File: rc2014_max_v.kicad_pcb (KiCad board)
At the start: 4 copper layers, 101.6 x 50.8 mm, 128 parts, among them J1 M3 Mounting Hole, J2 Conn_01x40, J3 Conn_01x24, J4 USB_B_Micro, J5 AVR-JTAG-10, J6 Pro Bus, J7 PMOD1, J8 PMOD2, J9 UPDI TTL, SW1 SW_Push, SW2 SW_Push, U1 TXB0108PWR, U10 ATtiny1614-SS, U11 5M1270ZT144C5N, U12 93LC46BT-I/OT, U13 IS61LV5128AL-10TLI, U14 Si5351A-B-GT, U15 TXB0108PWR, U16 TXB0108PWR, U17 MIC5356-SGYMME, U2 TXB0108PWR, U3 TXB0108PWR, U4 TXB0108PWR, U5 TXB0108PWR, U6 TXB0108PWR, U7 TXB0108PWR, U8 TPD2EUSB30, U9 FT2232H, X1 KC5032K12.0000C10E00, Y1 25MHZ 8PF

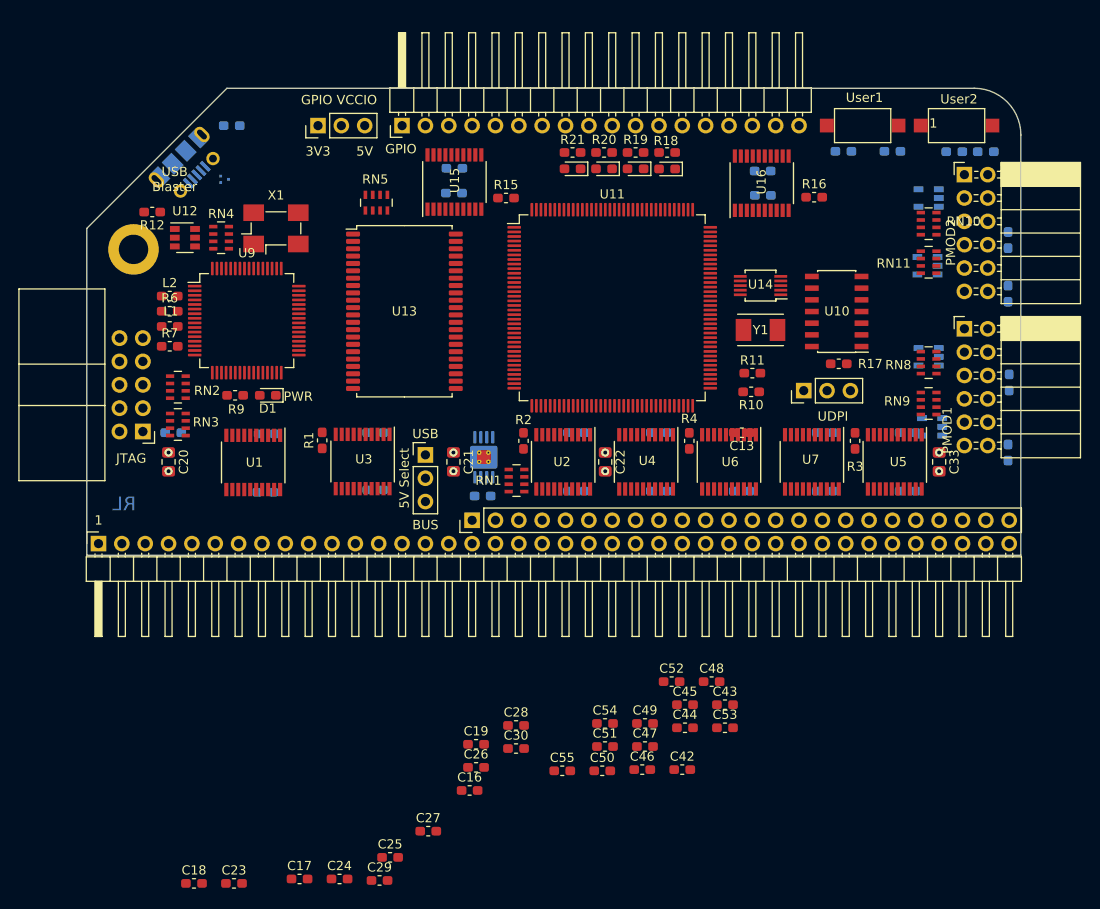
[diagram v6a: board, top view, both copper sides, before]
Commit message: placed all parts
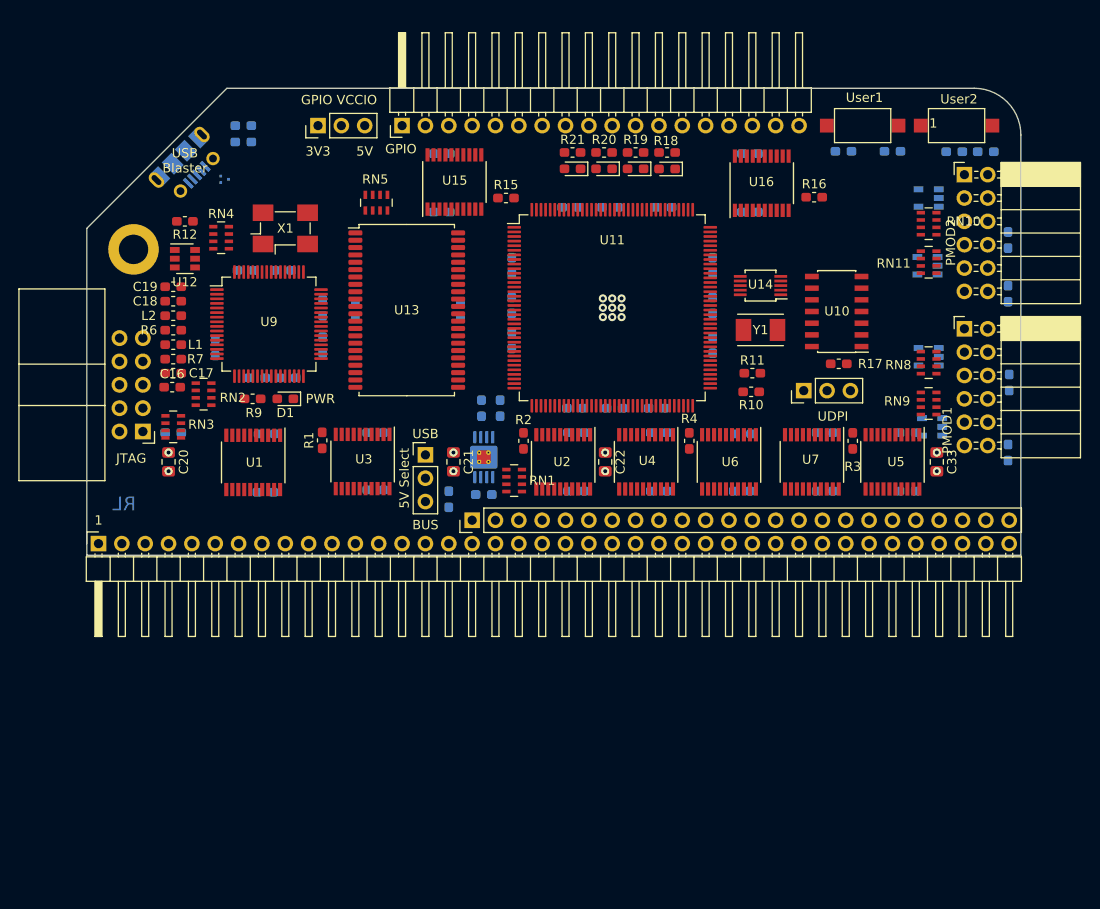
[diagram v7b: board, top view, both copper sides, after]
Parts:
- added C56: 100nF, Capacitor_SMD:C_0603_1608Metric_Pad1.05x0.95mm_HandSolder, B.Cu at (121.7, 104.1)
- added C57: 100nF, Capacitor_SMD:C_0603_1608Metric_Pad1.05x0.95mm_HandSolder, B.Cu at (104.6, 100.8)
- added C58: 100nF, Capacitor_SMD:C_0603_1608Metric_Pad1.05x0.95mm_HandSolder, B.Cu at (116.1, 100.8)
- C13, C23, C24, C25, C26, C27, C28, C29, C30, C42, C43, C44, C45, C46, C47, C48, C49, C50, C51, C52, C53, C54, C55: moved to B.Cu
- moved C23 80.7 mm to (92.5, 82.5)
- moved C29 67.9 mm to (92.7, 96.5)
- moved C24 66.5 mm to (96.8, 96.5)
- moved C18 63.4 mm to (84.8, 99.9), turned to 180 degrees
- moved C25 60.2 mm to (101.1, 100.6), turned to 90 degrees
- moved C19 59.7 mm to (84.8, 98.3), turned to 180 degrees
- moved C17 56.7 mm to (84.8, 107.7), turned to 180 degrees
- moved C45 55.5 mm to (128.0, 89.7)
- moved C30 54.5 mm to (89.4, 104.9), turned to 270 degrees
- moved C16 54.5 mm to (84.7, 109.2)
- moved C51 53.3 mm to (121.7, 96.0), turned to 270 degrees
- moved C52 52.0 mm to (132.3, 89.7)
- moved C48 51.9 mm to (138.2, 89.7)
- moved C27 51.6 mm to (97.3, 108.2), turned to 180 degrees
- moved C53 51.5 mm to (121.7, 100.3), turned to 90 degrees
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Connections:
- RN1 pad 5: 3V3 -> 5V
- RN1 pad 6: 3V3 -> 5V
- RN1 pad 7: 3V3 -> 5V
- RN1 pad 8: 3V3 -> 5V
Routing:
- net GND: vias 0 -> 9

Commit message: Added bus structure, additional pins added, 5V load balancer
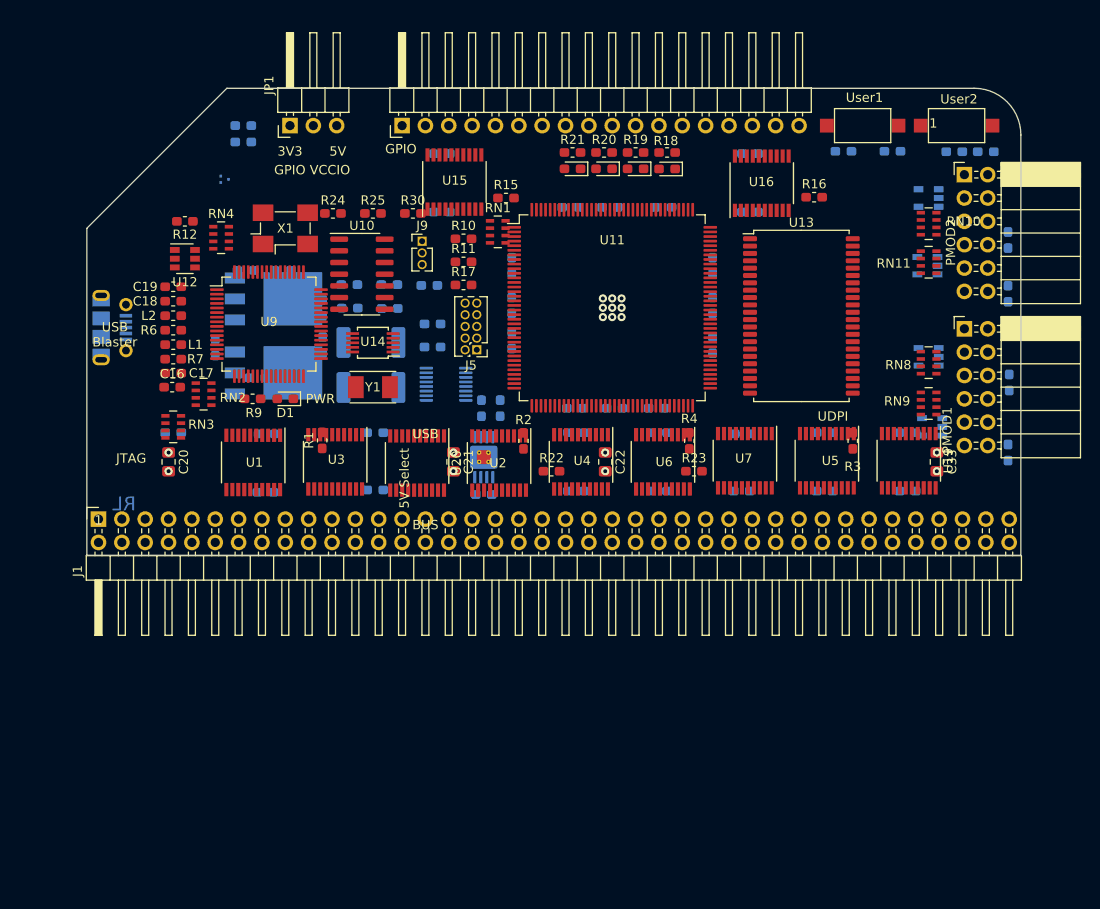
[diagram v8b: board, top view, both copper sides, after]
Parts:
- removed J2: Conn_01x40, Connector_PinHeader_2.54mm:PinHeader_1x40_P2.54mm_Horizontal
- removed J3: Conn_01x24, Connector_PinHeader_2.54mm:PinHeader_1x24_P2.54mm_Vertical
- removed JP2: Jumper_3_Bridged12, Connector_PinHeader_2.54mm:PinHeader_1x03_P2.54mm_Vertical
- removed RN5: 10K, Resistor_SMD:R_Array_Concave_4x0603
- added C59: 39nF, Capacitor_SMD:C_0603_1608Metric_Pad1.05x0.95mm_HandSolder, B.Cu at (108.3, 98.1)
- added D2: LED, LED_SMD:LED_0603_1608Metric_Pad1.05x0.95mm_HandSolder, B.Cu at (104.0, 100.6)
- added Q1: IRLR8726PBF, Package_TO_SOT_SMD:TO-252-3_TabPin4, B.Cu at (95.7, 107.7)
- added Q2: IRLR8726PBF, Package_TO_SOT_SMD:TO-252-3_TabPin4, B.Cu at (95.7, 99.6)
- added R22: 10K, Resistor_SMD:R_0603_1608Metric_Pad1.05x0.95mm_HandSolder, F.Cu at (126.0, 118.4)
- added R23: 10K, Resistor_SMD:R_0603_1608Metric_Pad1.05x0.95mm_HandSolder, F.Cu at (141.5, 118.4)
- added R24: 10K, Resistor_SMD:R_0603_1608Metric_Pad1.05x0.95mm_HandSolder, F.Cu at (102.2, 90.3)
- added R25: 10K, Resistor_SMD:R_0603_1608Metric_Pad1.05x0.95mm_HandSolder, F.Cu at (106.6, 90.3)
- added R26: 2.5m, Resistor_SMD:R_2512_6332Metric_Pad1.52x3.35mm_HandSolder, B.Cu at (106.3, 109.3)
- added R27: 820R, Resistor_SMD:R_0603_1608Metric_Pad1.05x0.95mm_HandSolder, B.Cu at (113.0, 102.3)
- added R28: 2.5m, Resistor_SMD:R_2512_6332Metric_Pad1.52x3.35mm_HandSolder, B.Cu at (106.3, 104.4)
- added R29: 30.1k, Resistor_SMD:R_0603_1608Metric_Pad1.05x0.95mm_HandSolder, B.Cu at (112.7, 98.2)
- added R30: 1K, Resistor_SMD:R_0603_1608Metric_Pad1.05x0.95mm_HandSolder, F.Cu at (110.9, 90.3)
- added U18: LTC4370, Package_SO:MSOP-16_3x4.039mm_P0.5mm, B.Cu at (114.5, 108.9)
- added U19: TXB0108PWR, Package_SO:TSSOP-20_4.4x6.5mm_P0.65mm, F.Cu at (164.8, 117.2)
- added U20: TXB0108PWR, Package_SO:TSSOP-20_4.4x6.5mm_P0.65mm, F.Cu at (111.4, 117.5)
- C15: value 100nF -> 39nF
- J1: value M3 Mounting Hole -> RC80 Bus; footprint MountingHole:MountingHole_3.2mm_M3_ISO14580_Pad -> Connector_PinHeader_2.54mm:PinHeader_2x40_Top_Bottom_P2.54mm_Horizontal
- J5: footprint Connector_IDC:IDC-Header_2x05_P2.54mm_Horizontal -> Connector_PinHeader_1.27mm:PinHeader_2x05_P1.27mm_Vertical
- J6: value Pro Bus -> GPIO
- J9: footprint Connector_PinHeader_2.54mm:PinHeader_1x03_P2.54mm_Vertical -> Connector_PinHeader_1.27mm:PinHeader_1x03_P1.27mm_Vertical
- JP1: footprint Connector_PinHeader_2.54mm:PinHeader_1x03_P2.54mm_Vertical -> Connector_PinHeader_2.54mm:PinHeader_1x03_P2.54mm_Horizontal
- moved U10 51.8 mm to (105.4, 96.9), turned to 0 degrees
- moved J9 44.6 mm to (111.9, 93.3), turned to 0 degrees
- moved U13 42.9 mm to (153.2, 101.5)
- moved U14 42.6 mm to (106.6, 104.4)
- moved Y1 42.6 mm to (106.6, 109.2)
- moved R17 41.7 mm to (116.4, 98.1)
- moved J5 37.4 mm to (117.9, 105.2)
- moved R10 35.4 mm to (116.4, 93.1), turned to 0 degrees
- moved J1 34.6 mm to (76.7, 128.7), turned to 90 degrees
- moved R11 33.7 mm to (116.4, 95.6), turned to 0 degrees
- moved RN1 27.1 mm to (120.1, 92.3), turned to 0 degrees
- moved C15 25.7 mm to (104.0, 98.1), turned to 0 degrees
- moved J4 19.4 mm to (78.2, 102.7), turned to 90 degrees
- moved C57 9.31 mm to (113.0, 104.9), turned to 0 degrees
- moved C58 7.70 mm to (108.4, 100.7), turned to 0 degrees
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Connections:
- net 1V8 renamed +1V8
- C1 pad 1: 5V -> +5V
- C10 pad 1: 3V3 -> +3V3
- C11 pad 1: 3V3 -> +3V3
- C12 pad 1: 3V3 -> +3V3
- C13 pad 1: 3V3 -> +3V3
- C14 pad 1: 3V3 -> +3V3
- C15 pad 1: GND -> 5V_U
- C15 pad 2: 5V_R -> Net-(C15-Pad2)
- C2 pad 1: 5V -> +5V
- C20 pad 1: 3V3 -> +3V3
- C20 pad 2: 5V -> +5V
- C21 pad 1: 3V3 -> +3V3
- C21 pad 2: 5V -> +5V
- C22 pad 1: 3V3 -> +3V3
- C22 pad 2: 5V -> +5V
- C24 pad 1: 3V3 -> +3V3
- C25 pad 1: 3V3 -> +3V3
- C26 pad 1: 3V3 -> +3V3
- C27 pad 1: 3V3 -> +3V3
- C3 pad 1: 5V -> +5V
- C31 pad 1: 3V3 -> +3V3
- C32 pad 1: 3V3 -> +3V3
- C33 pad 1: 3V3 -> +3V3
- C33 pad 2: 5V -> +5V
- C38 pad 1: 3V3 -> +3V3
- C39 pad 1: 3V3 -> +3V3
- C4 pad 1: 5V -> +5V
- C40 pad 1: 3V3 -> +3V3
- C41 pad 1: 3V3 -> +3V3
- C43 pad 1: 5V -> +5V
- C44 pad 1: 3V3 -> +3V3
- C45 pad 1: 3V3 -> +3V3
- C46 pad 1: 3V3 -> +3V3
- C47 pad 1: 3V3 -> +3V3
- C48 pad 1: 3V3 -> +3V3
- C49 pad 1: 3V3 -> +3V3
- C5 pad 1: 5V -> +5V
- C50 pad 1: 3V3 -> +3V3
- C51 pad 1: 3V3 -> +3V3
- C56 pad 1: 3V3 -> +3V3
- C57 pad 1: 3V3 -> Net-(C57-Pad1)
- C58 pad 1: 3V3 -> Net-(C58-Pad1)
- C6 pad 1: 5V -> +5V
- C7 pad 1: 5V -> +5V
- C8 pad 1: 3V3 -> +3V3
- C9 pad 1: 3V3 -> +3V3
- J1 pad 1: GND -> /A15
- J5 pad 4: 3V3 -> +3V3
- J5 pad 6: 3V3 -> +3V3
- J7 pad 12: 3V3 -> +3V3
- J7 pad 6: 3V3 -> +3V3
- J8 pad 12: 3V3 -> +3V3
- J8 pad 6: 3V3 -> +3V3
- JP1 pad 1: 3V3 -> +3V3
- JP1 pad 3: 5V -> +5V
- L1 pad 1: 3V3 -> +3V3
- L2 pad 1: 3V3 -> +3V3
- R10 pad 1: 3V3 -> +3V3
- R11 pad 1: 3V3 -> +3V3
- R13 pad 1: 3V3 -> +3V3
- R14 pad 1: 3V3 -> +3V3
- R18 pad 1: 3V3 -> +3V3
- R19 pad 1: 3V3 -> +3V3
- R20 pad 1: 3V3 -> +3V3
- R21 pad 1: 3V3 -> +3V3
- R7 pad 1: 3V3 -> +3V3
- R9 pad 1: 3V3 -> +3V3
- RN1 pad 1: ~INT -> ~CE~_RAM
- RN1 pad 2: ~NMI -> ~WE~_RAM
- RN1 pad 3: ~WAIT -> ~OE~_RAM
- RN1 pad 4: ~BUSRQ -> (no net)
- RN1 pad 5: 5V -> +3V3
- RN1 pad 6: 5V -> +3V3
- RN1 pad 7: 5V -> +3V3
- RN1 pad 8: 5V -> +3V3
- RN3 pad 6: 3V3 -> +3V3
- RN3 pad 7: 3V3 -> +3V3
- RN3 pad 8: 3V3 -> +3V3
- RN4 pad 5: 3V3 -> +3V3
- RN4 pad 6: 3V3 -> +3V3
- RN4 pad 7: 3V3 -> +3V3
- RN4 pad 8: 3V3 -> +3V3
- U1 pad 12: A15 -> /A15
- U1 pad 13: A14 -> /A14
- U1 pad 14: A13 -> /A13
- U1 pad 15: A12 -> /A12
- U1 pad 16: A11 -> /A11
- U1 pad 17: A10 -> /A10
- U1 pad 18: A9 -> /A9
- U1 pad 19: 5V -> +5V
- U1 pad 2: 3V3 -> +3V3
- U1 pad 20: A8 -> /A8
- U10 pad 1: 3V3 -> +3V3
- U11 pad 1: (no net) -> A17_F
- U11 pad 100: 3V3 -> +3V3
- U11 pad 116: 3V3 -> +3V3
- U11 pad 119: (no net) -> LED4
- U11 pad 120: (no net) -> LED3
- U11 pad 121: (no net) -> LED2
- U11 pad 122: (no net) -> LED1
- U11 pad 123: LED4 -> GPIO_8_F
- U11 pad 124: LED3 -> GPIO_7_F
- U11 pad 125: LED2 -> GPIO_6_F
- U11 pad 127: LED1 -> GPIO_5_F
- U11 pad 129: (no net) -> GPIO_4_F
- U11 pad 130: (no net) -> GPIO_3_F
- U11 pad 131: (no net) -> GPIO_2_F
- U11 pad 132: (no net) -> GPIO_1_F
- U11 pad 133: (no net) -> OE_G
- U11 pad 134: GPIO_8_F -> (no net)
- U11 pad 136: 3V3 -> +3V3
- U11 pad 137: GPIO_7_F -> (no net)
- U11 pad 138: GPIO_6_F -> (no net)
- U11 pad 139: GPIO_5_F -> A23_F
- U11 pad 140: GPIO_4_F -> A22_F
- U11 pad 141: GPIO_3_F -> A21_F
- U11 pad 142: GPIO_2_F -> A20_F
- U11 pad 143: GPIO_1_F -> A19_F
- U11 pad 144: OE_G -> A18_F
- U11 pad 2: (no net) -> A16_F
- U11 pad 25: 3V3 -> +3V3
- U11 pad 46: 3V3 -> +3V3
- U11 pad 64: 3V3 -> +3V3
- U11 pad 82: 3V3 -> +3V3
- U11 pad 9: 3V3 -> +3V3
- U12 pad 6: 3V3 -> +3V3
- U13 pad 11: 3V3 -> +3V3
- U13 pad 33: 3V3 -> +3V3
- U13 pad 39: (no net) -> A16_F
- U13 pad 40: (no net) -> A17_F
- U13 pad 41: (no net) -> A18_F
- U14 pad 1: 3V3 -> +3V3
- U14 pad 7: 3V3 -> +3V3
- U15 pad 2: 3V3 -> +3V3
- U16 pad 2: 3V3 -> +3V3
- U17 pad 1: 5V -> +5V
- U17 pad 3: (no net) -> +5V
- U17 pad 4: 5V -> +5V
- U17 pad 5: 5V -> +5V
- U17 pad 8: 3V3 -> +3V3
- U2 pad 12: ~RFSH -> /~RFSH
- U2 pad 13: ~M1 -> /~M1
- U2 pad 14: ~PAGE -> /~PAGE
- U2 pad 15: ~RESET -> /~RESET
- U2 pad 16: CLK2 -> /CLK2
- U2 pad 17: CLK -> /CLK
- U2 pad 18: ~INT -> /~INT
- U2 pad 19: 5V -> +5V
- U2 pad 2: 3V3 -> +3V3
- U2 pad 20: ~BUSACK -> /~BUSACK
- U3 pad 12: A7 -> /A7
- U3 pad 13: A6 -> /A6
- U3 pad 14: A5 -> /A5
- U3 pad 15: A4 -> /A4
- U3 pad 16: A3 -> /A3
- U3 pad 17: A2 -> /A2
- U3 pad 18: A1 -> /A1
- U3 pad 19: 5V -> +5V
- U3 pad 2: 3V3 -> +3V3
- U3 pad 20: A0 -> /A0
- U4 pad 12: ~HALT -> /~HALT
- U4 pad 13: ~MREQ -> /~MREQ
- U4 pad 14: ~BUSRQ -> /~BUSREQ
- U4 pad 15: ~WR -> /~WR
- U4 pad 16: ~WAIT -> /~WAIT
- U4 pad 17: ~RD -> /~RD
- U4 pad 18: ~IORQ -> /~IORQ
- U4 pad 19: 5V -> +5V
- U4 pad 2: 3V3 -> +3V3
- U4 pad 20: ~NMI -> /~NMI
- U5 pad 12: GND -> (no net)
- U5 pad 13: GND -> /USR3
- U5 pad 14: GND -> /USR2
- U5 pad 15: GND -> /USR1
- U5 pad 16: TXB -> /RXB
- U5 pad 17: TXA -> /TXB
- U5 pad 18: RXB -> /RXA
- U5 pad 19: 5V -> +5V
- U5 pad 2: 3V3 -> +3V3
- U5 pad 20: RXA -> /TXA
- U5 pad 6: GND -> (no net)
- U5 pad 7: GND -> (no net)
- U5 pad 8: GND -> (no net)
- U5 pad 9: GND -> (no net)
- U6 pad 12: D8 -> /D8
- U6 pad 13: D0 -> /D0
- U6 pad 14: D9 -> /D9
- U6 pad 15: D1 -> /D1
- U6 pad 16: D10 -> /D10
- U6 pad 17: D2 -> /D2
- U6 pad 18: D11 -> /D11
- U6 pad 19: 5V -> +5V
- U6 pad 2: 3V3 -> +3V3
- U6 pad 20: D3 -> /D3
- U7 pad 12: D12 -> /D12
- U7 pad 13: D4 -> /D4
- U7 pad 14: D13 -> /D13
- U7 pad 15: D5 -> /D5
- U7 pad 16: D14 -> /D14
- U7 pad 17: D6 -> /D6
- U7 pad 18: D15 -> /D15
- U7 pad 19: 5V -> +5V
- U7 pad 2: 3V3 -> +3V3
- U7 pad 20: D7 -> /D7
- U9 pad 20: 3V3 -> +3V3
- U9 pad 31: 3V3 -> +3V3
- U9 pad 42: 3V3 -> +3V3
- U9 pad 56: 3V3 -> +3V3
- X1 pad 1: 3V3 -> +3V3
- X1 pad 4: 3V3 -> +3V3
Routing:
- net 5V: vias 4 -> 0
- net 3V3: vias 4 -> 0
- net +5V: vias 0 -> 4
- net +3V3: vias 0 -> 4
- added copper zone on In1.Cu, net +3V3
- removed copper zone on In1.Cu, net 3V3
